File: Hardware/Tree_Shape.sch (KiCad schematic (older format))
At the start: 162 parts

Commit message: Replaced trunk through-hole resistors by SMD ones.
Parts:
- R69, R70, R71, R72, R73, R74, R75, R76, R77, R78, R79, R80, R81: footprint Resistor_THT:R_Axial_DIN0207_L6.3mm_D2.5mm_P7.62mm_Horizontal -> Resistor_SMD:R_1206_3216Metric_Pad1.42x1.75mm_HandSolder
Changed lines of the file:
@@
 F 0 "R69" H 1320 6346 50  0000 L CNN
 F 1 "180" H 1320 6255 50  0000 L CNN
-F 2 "Resistor_THT:R_Axial_DIN0207_L6.3mm_D2.5mm_P7.62mm_Horizontal" V 1180 6300 50  0001 C CNN
+F 2 "Resistor_SMD:R_1206_3216Metric_Pad1.42x1.75mm_HandSolder" V 1180 6300 50  0001 C CNN
 F 3 "~" H 1250 6300 50  0001 C CNN
 	1    1250 6300
@@
 F 0 "R70" H 1670 6346 50  0000 L CNN
 F 1 "180" H 1670 6255 50  0000 L CNN
-F 2 "Resistor_THT:R_Axial_DIN0207_L6.3mm_D2.5mm_P7.62mm_Horizontal" V 1530 6300 50  0001 C CNN
+F 2 "Resistor_SMD:R_1206_3216Metric_Pad1.42x1.75mm_HandSolder" V 1530 6300 50  0001 C CNN
 F 3 "~" H 1600 6300 50  0001 C CNN
 	1    1600 6300
@@
 F 0 "R71" H 2020 6346 50  0000 L CNN
 F 1 "180" H 2020 6255 50  0000 L CNN
-F 2 "Resistor_THT:R_Axial_DIN0207_L6.3mm_D2.5mm_P7.62mm_Horizontal" V 1880 6300 50  0001 C CNN
+F 2 "Resistor_SMD:R_1206_3216Metric_Pad1.42x1.75mm_HandSolder" V 1880 6300 50  0001 C CNN
 F 3 "~" H 1950 6300 50  0001 C CNN
 	1    1950 6300
@@
 F 0 "R72" H 2370 6346 50  0000 L CNN
 F 1 "180" H 2370 6255 50  0000 L CNN
-F 2 "Resistor_THT:R_Axial_DIN0207_L6.3mm_D2.5mm_P7.62mm_Horizontal" V 2230 6300 50  0001 C CNN
+F 2 "Resistor_SMD:R_1206_3216Metric_Pad1.42x1.75mm_HandSolder" V 2230 6300 50  0001 C CNN
 F 3 "~" H 2300 6300 50  0001 C CNN
 	1    2300 6300
@@
 F 0 "R73" H 2720 6346 50  0000 L CNN
 F 1 "180" H 2720 6255 50  0000 L CNN
-F 2 "Resistor_THT:R_Axial_DIN0207_L6.3mm_D2.5mm_P7.62mm_Horizontal" V 2580 6300 50  0001 C CNN
+F 2 "Resistor_SMD:R_1206_3216Metric_Pad1.42x1.75mm_HandSolder" V 2580 6300 50  0001 C CNN
 F 3 "~" H 2650 6300 50  0001 C CNN
 	1    2650 6300
@@
 F 0 "R74" H 3070 6346 50  0000 L CNN
 F 1 "180" H 3070 6255 50  0000 L CNN
-F 2 "Resistor_THT:R_Axial_DIN0207_L6.3mm_D2.5mm_P7.62mm_Horizontal" V 2930 6300 50  0001 C CNN
+F 2 "Resistor_SMD:R_1206_3216Metric_Pad1.42x1.75mm_HandSolder" V 2930 6300 50  0001 C CNN
 F 3 "~" H 3000 6300 50  0001 C CNN
 	1    3000 6300
@@
 F 0 "R75" H 3420 6346 50  0000 L CNN
 F 1 "180" H 3420 6255 50  0000 L CNN
-F 2 "Resistor_THT:R_Axial_DIN0207_L6.3mm_D2.5mm_P7.62mm_Horizontal" V 3280 6300 50  0001 C CNN
+F 2 "Resistor_SMD:R_1206_3216Metric_Pad1.42x1.75mm_HandSolder" V 3280 6300 50  0001 C CNN
 F 3 "~" H 3350 6300 50  0001 C CNN
 	1    3350 6300
@@
 F 0 "R76" H 3770 6346 50  0000 L CNN
 F 1 "180" H 3770 6255 50  0000 L CNN
-F 2 "Resistor_THT:R_Axial_DIN0207_L6.3mm_D2.5mm_P7.62mm_Horizontal" V 3630 6300 50  0001 C CNN
+F 2 "Resistor_SMD:R_1206_3216Metric_Pad1.42x1.75mm_HandSolder" V 3630 6300 50  0001 C CNN
 F 3 "~" H 3700 6300 50  0001 C CNN
 	1    3700 6300
@@
 F 0 "R77" H 4120 6346 50  0000 L CNN
 F 1 "180" H 4120 6255 50  0000 L CNN
-F 2 "Resistor_THT:R_Axial_DIN0207_L6.3mm_D2.5mm_P7.62mm_Horizontal" V 3980 6300 50  0001 C CNN
+F 2 "Resistor_SMD:R_1206_3216Metric_Pad1.42x1.75mm_HandSolder" V 3980 6300 50  0001 C CNN
 F 3 "~" H 4050 6300 50  0001 C CNN
 	1    4050 6300
@@
 F 0 "R78" H 4470 6346 50  0000 L CNN
 F 1 "180" H 4470 6255 50  0000 L CNN
-F 2 "Resistor_THT:R_Axial_DIN0207_L6.3mm_D2.5mm_P7.62mm_Horizontal" V 4330 6300 50  0001 C CNN
+F 2 "Resistor_SMD:R_1206_3216Metric_Pad1.42x1.75mm_HandSolder" V 4330 6300 50  0001 C CNN
 F 3 "~" H 4400 6300 50  0001 C CNN
 	1    4400 6300
@@
 F 0 "R79" H 4820 6346 50  0000 L CNN
 F 1 "180" H 4820 6255 50  0000 L CNN
-F 2 "Resistor_THT:R_Axial_DIN0207_L6.3mm_D2.5mm_P7.62mm_Horizontal" V 4680 6300 50  0001 C CNN
+F 2 "Resistor_SMD:R_1206_3216Metric_Pad1.42x1.75mm_HandSolder" V 4680 6300 50  0001 C CNN
 F 3 "~" H 4750 6300 50  0001 C CNN
 	1    4750 6300
@@
 F 0 "R80" H 5170 6346 50  0000 L CNN
 F 1 "180" H 5170 6255 50  0000 L CNN
-F 2 "Resistor_THT:R_Axial_DIN0207_L6.3mm_D2.5mm_P7.62mm_Horizontal" V 5030 6300 50  0001 C CNN
+F 2 "Resistor_SMD:R_1206_3216Metric_Pad1.42x1.75mm_HandSolder" V 5030 6300 50  0001 C CNN
 F 3 "~" H 5100 6300 50  0001 C CNN
 	1    5100 6300
@@
 F 0 "R81" H 5520 6346 50  0000 L CNN
 F 1 "180" H 5520 6255 50  0000 L CNN
-F 2 "Resistor_THT:R_Axial_DIN0207_L6.3mm_D2.5mm_P7.62mm_Horizontal" V 5380 6300 50  0001 C CNN
+F 2 "Resistor_SMD:R_1206_3216Metric_Pad1.42x1.75mm_HandSolder" V 5380 6300 50  0001 C CNN
 F 3 "~" H 5450 6300 50  0001 C CNN
 	1    5450 6300

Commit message: Replaced tree foliage through-hole resistors by SMD ones.
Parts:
- R1, R10, R11, R12, R13, R14, R15, R16, R17, R18, R19, R2, R20, R21, R22, R23, R24, R25, R26, R27, R28, R29, R3, R30, R31, R32, R33, R34, R35, R36, R37, R38, R39, R4, R40, R41, R42, R43, R44, R45, R46, R47, R48, R49, R5, R50, R51, R52, R53, R54, R55, R56, R57, R58, R59, R6, R60, R61, R62, R63, R64, R65, R66, R67, R68, R7, R8, R9: footprint Resistor_THT:R_Axial_DIN0207_L6.3mm_D2.5mm_P7.62mm_Horizontal -> Resistor_SMD:R_1206_3216Metric_Pad1.42x1.75mm_HandSolder

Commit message: Converted all 1206 SMD footprints to KiCad 5.1.10 latest one in both schematic and PCB.
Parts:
- R1, R10, R11, R12, R13, R14, R15, R16, R17, R18, R19, R2, R20, R21, R22, R23, R24, R25, R26, R27, R28, R29, R3, R30, R31, R32, R33, R34, R35, R36, R37, R38, R39, R4, R40, R41, R42, R43, R44, R45, R46, R47, R48, R49, R5, R50, R51, R52, R53, R54, R55, R56, R57, R58, R59, R6, R60, R61, R62, R63, R64, R65, R66, R67, R68, R69, R7, R70, R71, R72, R73, R74, R75, R76, R77, R78, R79, R8, R80, R81, R9: footprint Resistor_SMD:R_1206_3216Metric_Pad1.42x1.75mm_HandSolder -> Resistor_SMD:R_1206_3216Metric_Pad1.30x1.75mm_HandSolder

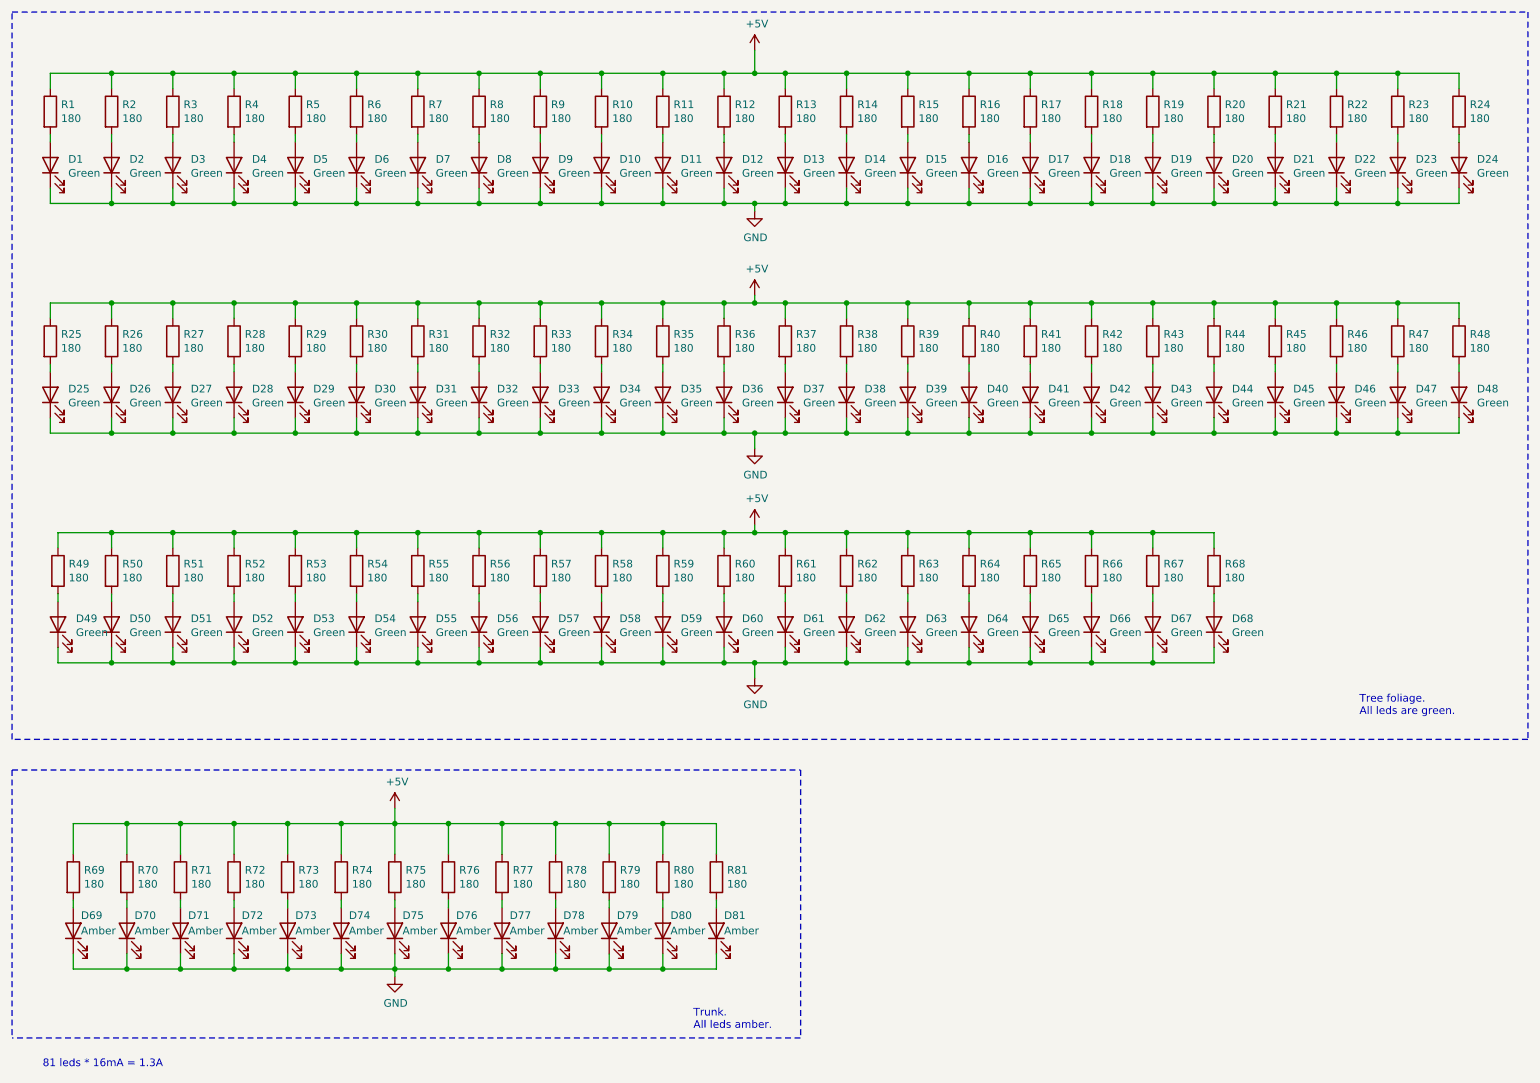
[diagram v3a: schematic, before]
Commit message: Updated bill of materials data on schematic to improve generated bill of materials.
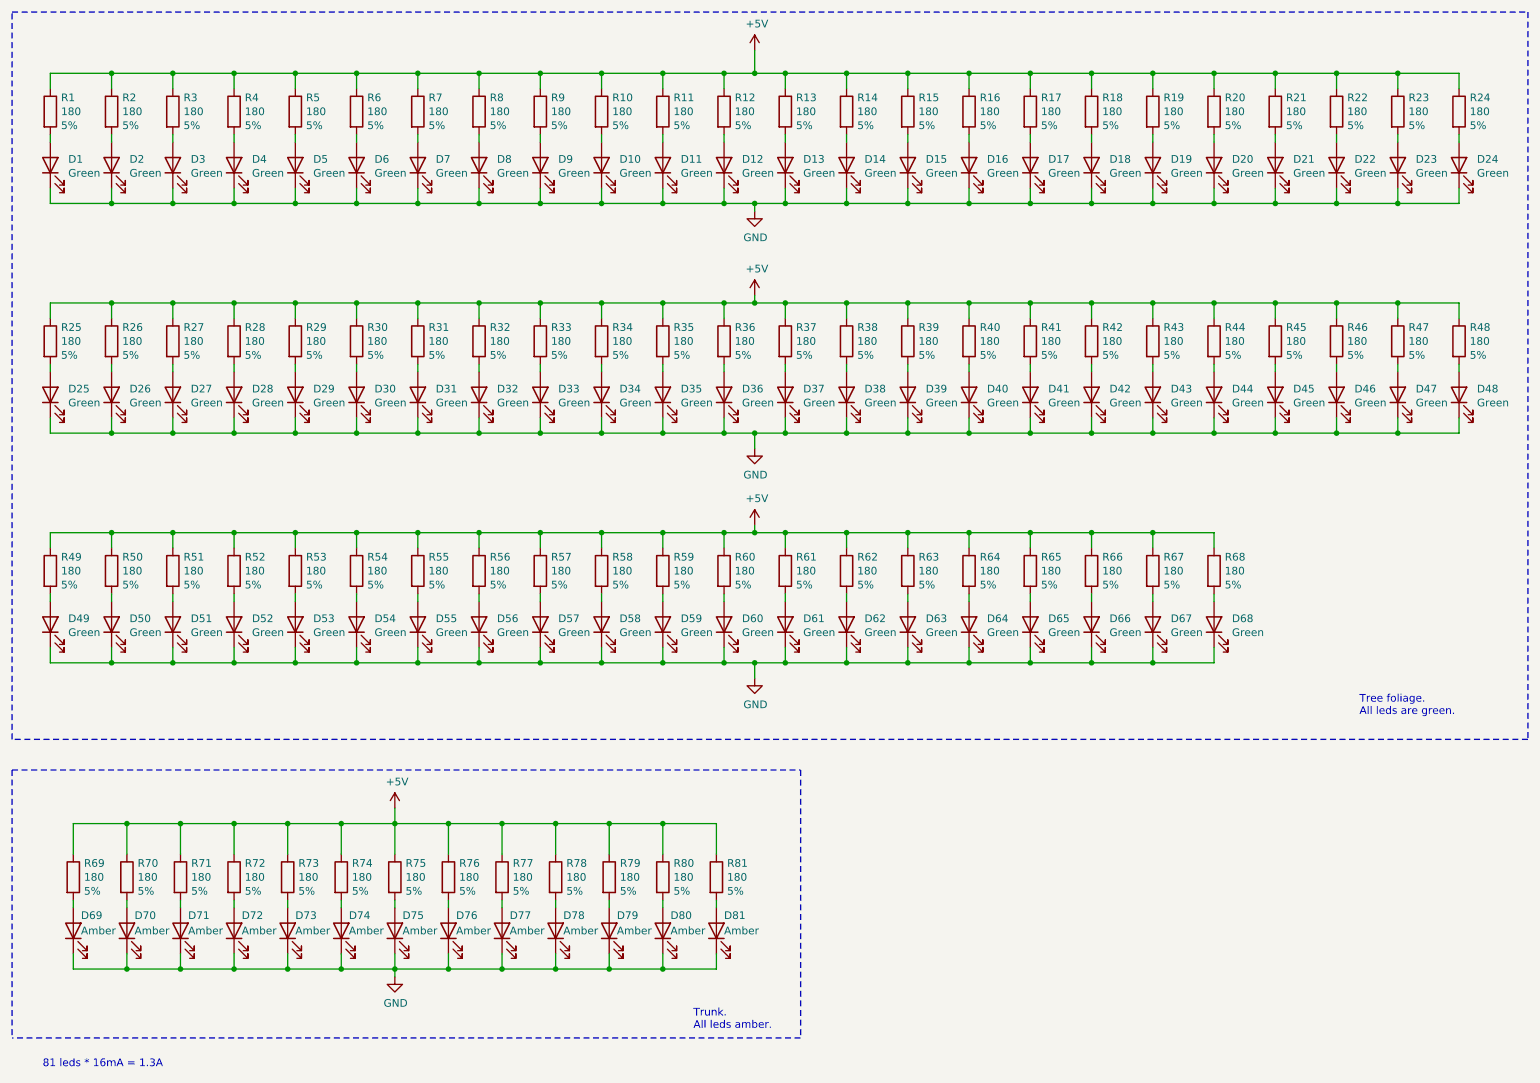
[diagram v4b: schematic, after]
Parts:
- R1, R10, R11, R12, R13, R14, R15, R16, R17, R18, R19, R2, R20, R21, R22, R23, R24, R25, R26, R27, R28, R29, R3, R30, R31, R32, R33, R34, R35, R36, R37, R38, R39, R4, R40, R41, R42, R43, R44, R45, R46, R47, R48, R49, R5, R50, R51, R52, R53, R54, R55, R56, R57, R58, R59, R6, R60, R61, R62, R63, R64, R65, R66, R67, R68, R69, R7, R70, R71, R72, R73, R74, R75, R76, R77, R78, R79, R8, R80, R81, R9: Value2 (none) -> 5%
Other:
- moved on the sheet: D49, R49
